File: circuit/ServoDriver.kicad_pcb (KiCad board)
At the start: 2 copper layers, 102.5 x 54.5 mm, 47 parts, among them IC1 TLP521, IC2 TLP521, IC3 TLP521, IC4 TLP521, IC5 TLP521, IC6 TLP521, J1 RJ45_8pin, J2 RJ45_8pin, J3 servo0, J4 servo1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

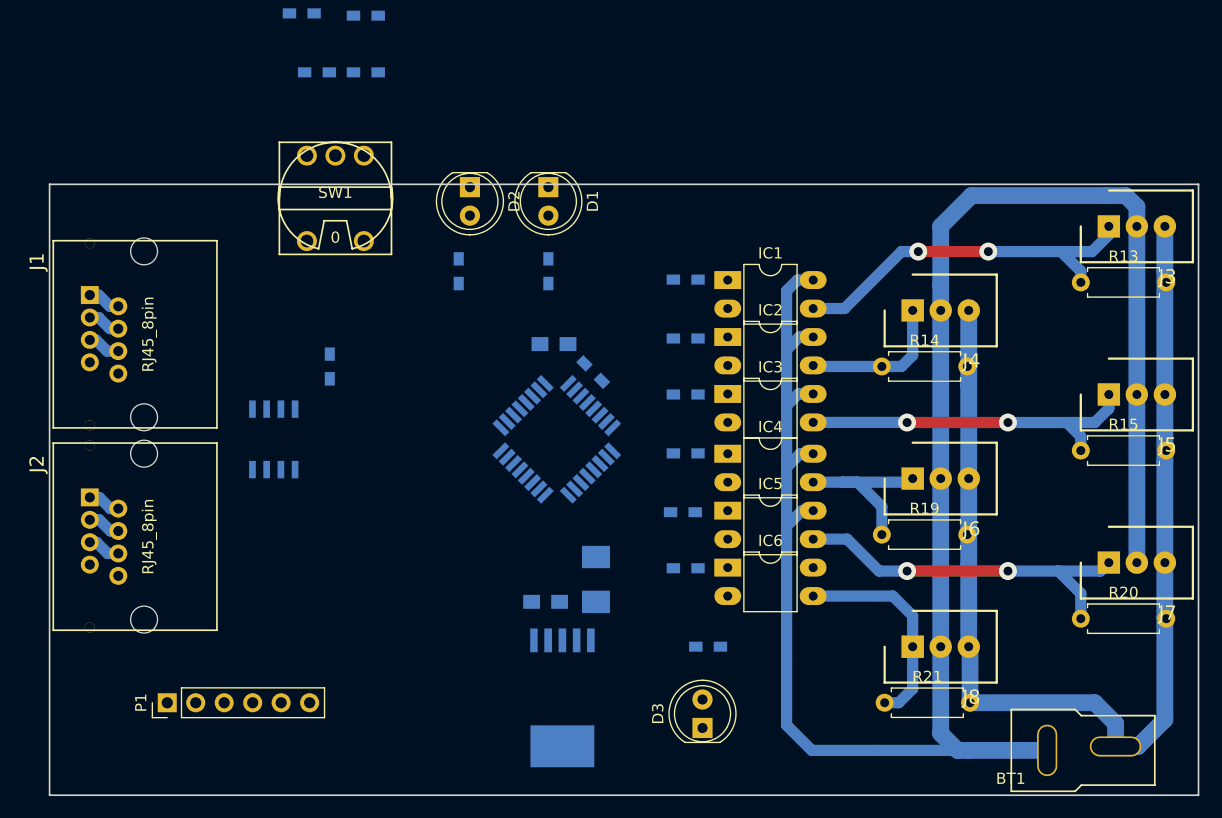
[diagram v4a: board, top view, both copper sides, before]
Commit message: ロータリースイッチとLEDのピンを変更
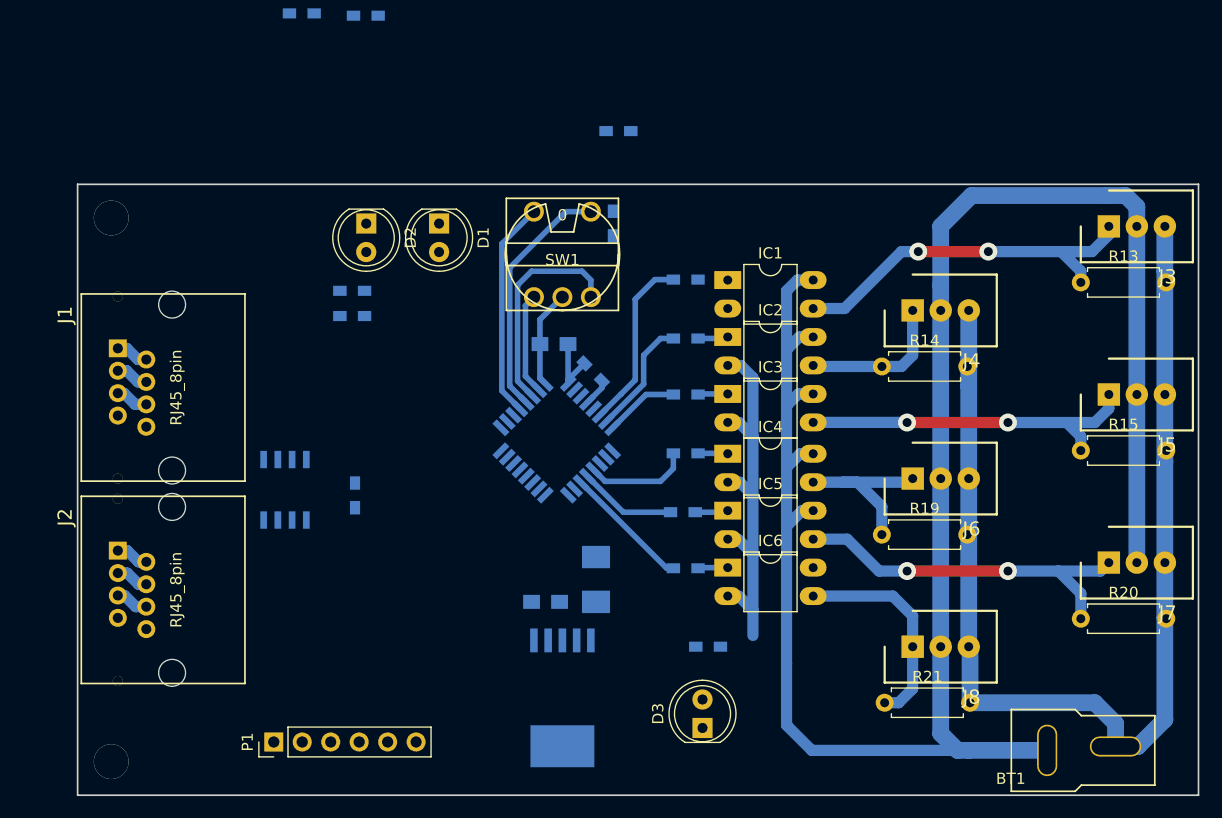
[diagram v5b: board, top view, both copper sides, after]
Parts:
- moved R9 27.4 mm to (132.2, 75.0)
- moved R7 25.8 mm to (131.8, 83.2), turned to 90 degrees
- moved SW1 20.9 mm to (127.2, 86.0), turned to 0 degrees
- moved R1 18.0 mm to (108.5, 91.5), turned to 0 degrees
- moved R5 11.7 mm to (108.8, 107.5)
- moved D1 10.3 mm to (116.2, 83.2)
- moved P1 10.1 mm to (101.5, 129.5)
- moved D2 9.80 mm to (109.8, 83.2)
- moved R2 9.66 mm to (108.5, 89.2), turned to 0 degrees
- moved J1 5.37 mm to (90.1, 97.9)
- moved J2 5.37 mm to (90.1, 115.9)
- moved U2 4.61 mm to (102.5, 107.0)
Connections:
- U1 pad 27: /RotarySW/BIT0 -> Net-(R1-Pad1)
- U1 pad 28: /RotarySW/BIT1 -> /RotarySW/BIT0
- U1 pad 29: /RotarySW/BIT2 -> /RotarySW/BIT1
- U1 pad 30: /RotarySW/BIT3 -> /RotarySW/BIT2
- U1 pad 31: Net-(R1-Pad1) -> /RotarySW/BIT3
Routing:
- net GND: track 6.20 -> 51.7 mm
- net /RotarySW/BIT1: track 0.00 -> 21.9 mm
- net /RotarySW/BIT0: track 0.00 -> 19.4 mm
- net /RotarySW/BIT2: track 0.00 -> 19.4 mm
- net /Servo0: track 0.00 -> 15.8 mm
- net /Servo5: track 0.00 -> 11.4 mm
- net /Servo1: track 0.00 -> 10.6 mm
- net /Servo3: track 0.00 -> 9.36 mm
- net /RotarySW/BIT3: track 0.00 -> 9.09 mm
- net /Servo4: track 0.00 -> 8.76 mm
- net /Servo2: track 0.00 -> 6.65 mm
- net +3V3: track 0.00 -> 5.92 mm
- net Net-(IC5-Pad1): track 0.00 -> 2.96 mm
- net Net-(IC2-Pad1): track 0.00 -> 2.71 mm
- net Net-(IC6-Pad1): track 0.00 -> 2.68 mm
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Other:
- board size 102.5 x 54.5 mm -> 100 x 54.5 mm

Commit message: ロータリースイッチの配線終わり
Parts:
- R9: footprint Resistors_SMD:R_0603_HandSoldering -> Resistors_THT:R_Axial_DIN0207_L6.3mm_D2.5mm_P7.62mm_Horizontal; moved to F.Cu
- moved R8 37.2 mm to (128.8, 92.2)
- moved R6 30.0 mm to (133.2, 83.2), turned to 90 degrees
- moved R9 17.5 mm to (132.2, 92.5), turned to 180 degrees
- moved R1 9.58 mm to (118.0, 90.2), turned to 90 degrees
- moved R2 1.46 mm to (109.8, 90.0), turned to 90 degrees
- moved C1 0.79 mm to (126.8, 94.8)
- moved R4 0.56 mm to (130.2, 97.0)
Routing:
- net +3V3: track 5.92 -> 21.7 mm
- net /RotarySW/BIT0: track 19.4 -> 29.7 mm
- net GND: track 51.7 -> 60.0 mm
- net Net-(IC1-Pad1): track 0.00 -> 2.67 mm
- net /RotarySW/BIT2: track 19.4 -> 21.8 mm
- net /RotarySW/BIT1: track 21.9 -> 23.9 mm

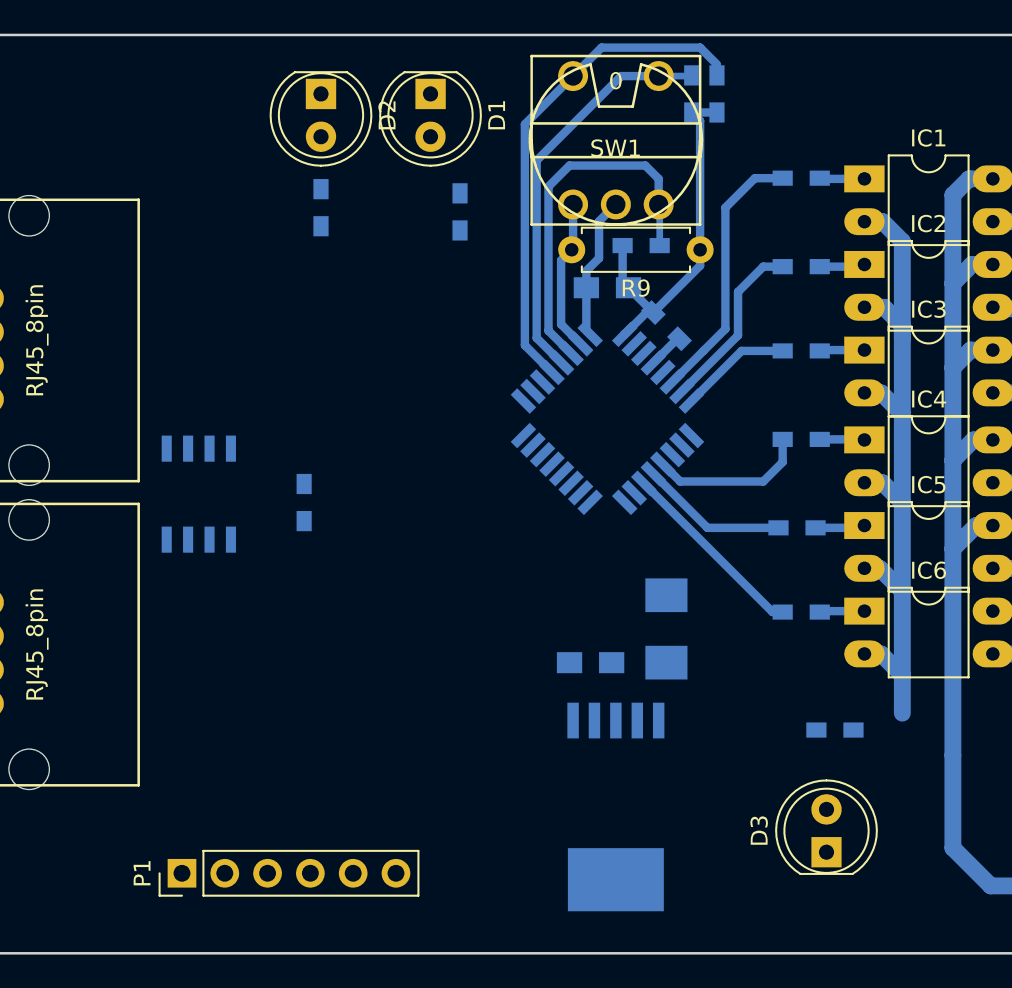
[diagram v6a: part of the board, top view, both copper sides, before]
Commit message: レギュレータまわりの配線完了
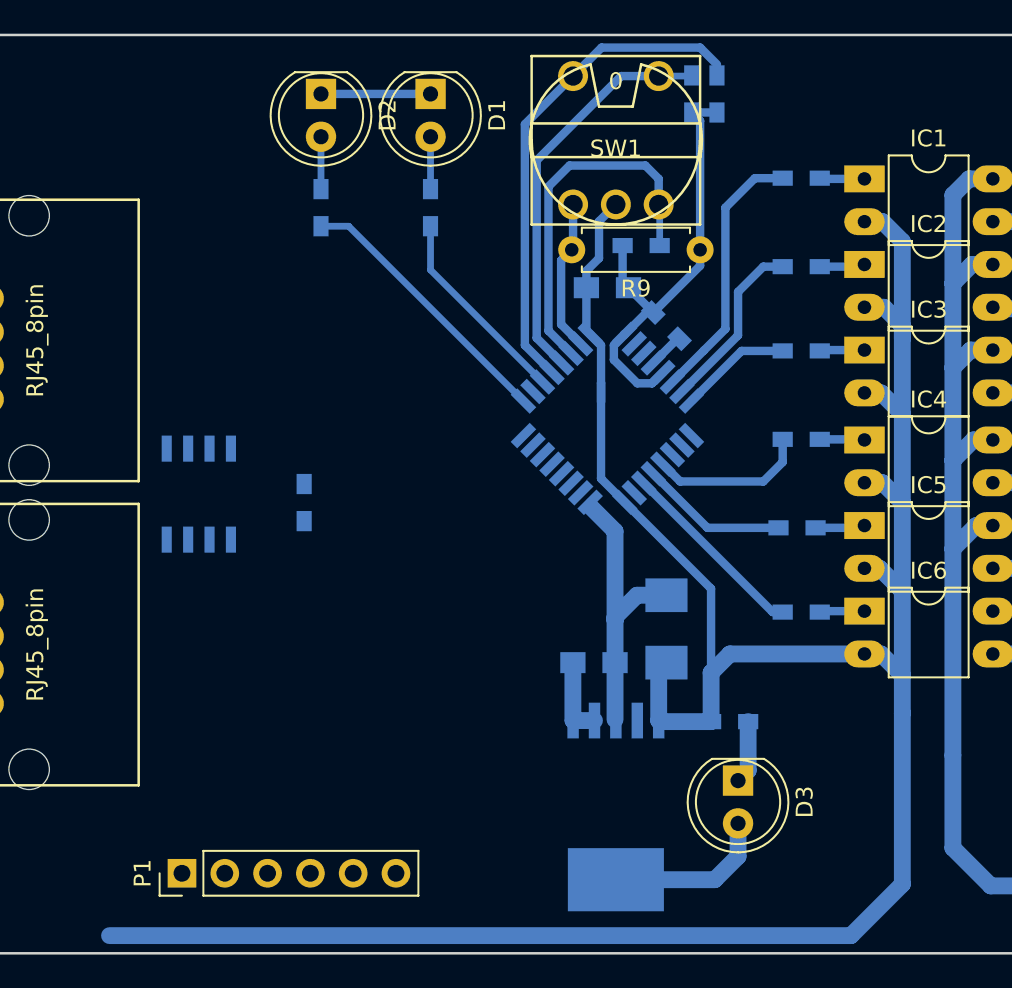
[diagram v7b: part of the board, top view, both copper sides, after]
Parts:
- moved D3 6.75 mm to (134.5, 124.0), turned to 270 degrees
- moved R3 6.27 mm to (134.0, 120.5)
- moved R1 1.77 mm to (116.2, 90.0)
- moved C2 0.20 mm to (126.0, 117.0)
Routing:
- net GND: track 60.0 -> 168.4 mm
- net +3V3: track 21.7 -> 54.4 mm
- net Net-(R2-Pad1): track 0.00 -> 16.3 mm
- net Net-(R1-Pad1): track 0.00 -> 12.0 mm
- net +5V: track 5.91 -> 10.6 mm
- net Net-(D3-Pad1): track 0.00 -> 3.75 mm
- net Net-(D2-Pad2): track 0.00 -> 3.11 mm
- net Net-(D1-Pad2): track 0.00 -> 3.11 mm
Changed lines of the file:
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@@
   (general
     (links 117)
-    (no_connects 42)
-    (area 83.924999 79.674999 184.075001 134.325001)
+    (no_connects 24)
+    (area 70.900002 77.034 191.176192 142.45)
     (thickness 1.6)
     (drawings 7)
-    (tracks 232)
+    (tracks 280)
     (zones 0)
     (modules 47)
@@
   )
   (module Capacitors_SMD:C_0805_HandSoldering (layer B.Cu)
-    (at 125.75 117)
+    (at 125.95 117)
     (descr "Capacitor SMD 0805, hand soldering")
     (tags "capacitor 0805")
@@
   )
   (module LEDs:LED_D5.0mm (layer F.Cu)
-    (at 139.75 128.25 90)
+    (at 134.5 124 270)
     (descr "LED, diameter 5.0mm, 2 pins, http://cdn-reichelt.de/documents/datenblatt/A500/LL-504BC2E-009.pdf")
     (tags "LED diameter 5.0mm 2 pins")
-    (fp_text reference D3 (at 1.27 -3.96 90) (layer F.SilkS)
-      (effects (font (size 1 1) (thickness 0.15)))
-    )
-    (fp_text value LED (at 1.27 3.96 90) (layer F.Fab)
+    (fp_text reference D3 (at 1.27 -3.96 270) (layer F.SilkS)
+      (effects (font (size 1 1) (thickness 0.15)))
+    )
+    (fp_text value LED (at 1.27 3.96 270) (layer F.Fab)
       (effects (font (size 1 1) (thickness 0.15)))
     )
@@
     (fp_line (start 4.5 3.25) (end 4.5 -3.25) (layer F.CrtYd) (width 0.05))
     (fp_line (start 4.5 -3.25) (end -1.95 -3.25) (layer F.CrtYd) (width 0.05))
-    (pad 1 thru_hole rect (at 0 0 90) (size 1.8 1.8) (drill 0.9) (layers *.Cu *.Mask)
+    (pad 1 thru_hole rect (at 0 0 270) (size 1.8 1.8) (drill 0.9) (layers *.Cu *.Mask)
       (net 8 "Net-(D3-Pad1)"))
-    (pad 2 thru_hole circle (at 2.54 0 90) (size 1.8 1.8) (drill 0.9) (layers *.Cu *.Mask)
+    (pad 2 thru_hole circle (at 2.54 0 270) (size 1.8 1.8) (drill 0.9) (layers *.Cu *.Mask)
       (net 3 +3V3))
     (model ${KISYS3DMOD}/LEDs.3dshapes/LED_D5.0mm.wrl
@@
   )
   (module Resistors_SMD:R_0603_HandSoldering (layer B.Cu)
-    (at 118 90.25 90)
+    (at 116.25 90 90)
     (descr "Resistor SMD 0603, hand soldering")
     (tags "resistor 0603")
@@
   )
   (module Resistors_SMD:R_0603_HandSoldering (layer B.Cu)
-    (at 140.25 121 180)
+    (at 134 120.5 180)
     (descr "Resistor SMD 0603, hand soldering")
     (tags "resistor 0603")
@@
   (segment (start 163.5 106) (end 163.5 97.75) (width 1.5) (layer B.Cu) (net 2))
   (segment (start 163.5 97.75) (end 163.5 91) (width 1.5) (layer B.Cu) (net 2))
+  (segment (start 125.724695 107.485103) (end 125.8 107.560408) (width 0.5) (layer B.Cu) (net 3) (status C00000))
+  (segment (start 125.8 107.560408) (end 125.8 107.8) (width 0.5) (layer B.Cu) (net 3) (status 400000))
+  (segment (start 125.8 107.8) (end 127.2 109.2) (width 1) (layer B.Cu) (net 3))
+  (segment (start 127.2 109.2) (end 127.2 114.5) (width 1) (layer B.Cu) (net 3))
+  (segment (start 127.2 117) (end 127.2 114.5) (width 1) (layer B.Cu) (net 3))
+  (segment (start 127.2 114.5) (end 127.2 114.3) (width 1) (layer B.Cu) (net 3))
+  (segment (start 128.5 113) (end 130.25 113) (width 1) (layer B.Cu) (net 3))
+  (segment (start 127.2 114.3) (end 128.5 113) (width 1) (layer B.Cu) (net 3))
+  (segment (start 134.5 126.54) (end 134.5 128.5) (width 1) (layer B.Cu) (net 3))
+  (segment (start 133.118 129.882) (end 127.25 129.882) (width 1) (layer B.Cu) (net 3))
+  (segment (start 134.5 128.5) (end 133.118 129.882) (width 1) (layer B.Cu) (net 3))
+  (segment (start 127.25052 120.4365) (end 127.2 120.38598) (width 0.5) (layer B.Cu) (net 3))
+  (segment (start 127.2 120.38598) (end 127.2 117) (width 1) (layer B.Cu) (net 3))
+  (segment (start 127.13084 99.03084) (end 128.522103 100.422103) (width 0.5) (layer B.Cu) (net 3))
+  (segment (start 128.522103 100.422103) (end 129.393583 100.422103) (width 0.5) (layer B.Cu) (net 3))
+  (segment (start 129.393583 100.422103) (end 129.401652 100.414034) (width 0.5) (layer B.Cu) (net 3))
+  (segment (start 129.401652 100.414034) (end 130.038047 99.777639) (width 0.5) (layer B.Cu) (net 3))
+  (segment (start 127.13084 98.159362) (end 127.13084 99.03084) (width 0.5) (layer B.Cu) (net 3))
+  (segment (start 127.775305 97.514897) (end 127.13084 98.159362) (width 0.5) (layer B.Cu) (net 3))
   (segment (start 127.775305 97.514897) (end 129.068019 96.222183) (width 0.5) (layer B.Cu) (net 3))
   (segment (start 131.75 84.35) (end 133.25 84.35) (width 0.5) (layer B.Cu) (net 3))
@@
   (segment (start 129.068019 96.222183) (end 129.472183 96.222183) (width 0.5) (layer B.Cu) (net 3))
   (segment (start 127.775305 97.514897) (end 127.75 97.489592) (width 0.5) (layer B.Cu) (net 3))
+  (segment (start 144.25 120) (end 144.25 130.15) (width 1) (layer B.Cu) (net 4))
+  (segment (start 144.25 117.75) (end 144.25 120) (width 1) (layer B.Cu) (net 4))
+  (segment (start 141.2 133.2) (end 97.2 133.2) (width 1) (layer B.Cu) (net 4))
+  (segment (start 144.25 130.15) (end 141.2 133.2) (width 1) (layer B.Cu) (net 4))
+  (segment (start 142.002 116.484) (end 134.016 116.484) (width 1) (layer B.Cu) (net 4) (status 400000))
+  (segment (start 134.016 116.484) (end 132.9 117.6) (width 1) (layer B.Cu) (net 4))
+  (segment (start 127.775305 107.485103) (end 132.9 112.609798) (width 0.5) (layer B.Cu) (net 4) (status 400000))
+  (segment (start 132.9 112.609798) (end 132.9 117.6) (width 0.5) (layer B.Cu) (net 4))
+  (segment (start 132.9 117.6) (end 132.9 120.5) (width 1) (layer B.Cu) (net 4) (status 800000))
+  (segment (start 132.9 120.5) (end 129.85402 120.5) (width 1) (layer B.Cu) (net 4))
+  (segment (start 129.85402 120.5) (end 129.79052 120.4365) (width 1) (layer B.Cu) (net 4))
+  (segment (start 129.79052 120.4365) (end 129.79052 117.45948) (width 1) (layer B.Cu) (net 4))
+  (segment (start 129.79052 117.45948) (end 130.25 117) (width 1) (layer B.Cu) (net 4))
+  (segment (start 126.36916 100.4) (end 126.36916 101.53084) (width 0.5) (layer B.Cu) (net 4))
+  (segment (start 126.36916 98.159362) (end 126.36916 100.4) (width 0.5) (layer B.Cu) (net 4))
+  (segment (start 126.36916 100.4) (end 126.36916 106.078958) (width 0.5) (layer B.Cu) (net 4))
+  (segment (start 126.36916 106.078958) (end 127.775305 107.485103) (width 0.5) (layer B.Cu) (net 4))
+  (segment (start 125.724695 97.514897) (end 126.36916 98.159362) (width 0.5) (layer B.Cu) (net 4))
+  (segment (start 109.75 83.25) (end 116.25 83.25) (width 0.5) (layer B.Cu) (net 4))
   (segment (start 144.25 97.75) (end 144.25 92) (width 1) (layer B.Cu) (net 4))
   (segment (start 144.25 92) (end 143.08 90.83) (width 1) (layer B.Cu) (net 4))
@@
   (segment (start 144.25 107.5) (end 144.25 112.75) (width 1) (layer B.Cu) (net 4))
   (segment (start 144.25 112.75) (end 144.25 117.75) (width 1) (layer B.Cu) (net 4))
-  (segment (start 144.25 117.75) (end 144.25 120) (width 1) (layer B.Cu) (net 4))
   (segment (start 87.59 116.43) (end 88.18 116.43) (width 1) (layer B.Cu) (net 4))
   (segment (start 88.18 116.43) (end 89.18 117.43) (width 1) (layer B.Cu) (net 4))
@@
   (segment (start 89.13 99.38) (end 90.13 99.38) (width 1) (layer B.Cu) (net 4))
   (segment (start 87.59 98.38) (end 87.88 98.38) (width 1) (layer B.Cu) (net 4))
+  (segment (start 125.98052 120.4365) (end 124.71052 120.4365) (width 1) (layer B.Cu) (net 5))
+  (segment (start 124.71052 120.4365) (end 124.7 120.42598) (width 0.5) (layer B.Cu) (net 5))
+  (segment (start 124.7 120.42598) (end 124.7 117) (width 1) (layer B.Cu) (net 5))
   (segment (start 87.59 114.43) (end 88.43 114.43) (width 1) (layer B.Cu) (net 5))
   (segment (start 88.43 114.43) (end 89.43 115.43) (width 1) (layer B.Cu) (net 5))
@@
   (segment (start 89.38 97.38) (end 88.38 96.38) (width 1) (layer B.Cu) (net 5))
   (segment (start 88.38 96.38) (end 87.59 96.38) (width 1) (layer B.Cu) (net 5))
+  (segment (start 116.25 85.79) (end 116.25 88.9) (width 0.4) (layer B.Cu) (net 6))
+  (segment (start 109.75 85.79) (end 109.75 88.9) (width 0.4) (layer B.Cu) (net 7))
+  (segment (start 135.1 120.5) (end 135.1 123.4) (width 1) (layer B.Cu) (net 8))
+  (segment (start 135.1 123.4) (end 134.5 124) (width 1) (layer B.Cu) (net 8))
   (segment (start 132.473528 98.473528) (end 133.75 97.197056) (width 0.5) (layer B.Cu) (net 9))
   (segment (start 133.75 90) (end 135.5 88.25) (width 0.5) (layer B.Cu) (net 9))
@@
   (segment (start 129.472361 99.211953) (end 130.906497 97.777817) (width 0.5) (layer B.Cu) (net 27))
   (segment (start 130.906497 97.777817) (end 131.027817 97.777817) (width 0.5) (layer B.Cu) (net 27))
+  (segment (start 116.25 91.1) (end 116.25 93.697056) (width 0.4) (layer B.Cu) (net 29))
+  (segment (start 116.25 93.697056) (end 122.896268 100.343324) (width 0.4) (layer B.Cu) (net 29))
+  (segment (start 121.764897 101.474695) (end 111.390202 91.1) (width 0.4) (layer B.Cu) (net 30))
+  (segment (start 111.390202 91.1) (end 109.75 91.1) (width 0.4) (layer B.Cu) (net 30))
   (segment (start 124.71 82.19) (end 126.4 80.5) (width 0.5) (layer B.Cu) (net 32))
   (segment (start 133.25 81.5) (end 133.25 82.15) (width 0.4) (layer B.Cu) (net 32))

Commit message: 配線完了
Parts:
- U2: footprint Housings_SOIC:SOIC-8_3.9x4.9mm_Pitch1.27mm -> Housings_DIP:DIP-8_W7.62mm_Socket_LongPads; moved to F.Cu
- moved U2 12.6 mm to (114.5, 111.0), turned to 180 degrees
- moved J1 7.87 mm to (98.0, 98.0), turned to 270 degrees
- moved J2 7.87 mm to (98.0, 116.0), turned to 270 degrees
- moved P1 5.10 mm to (96.5, 128.5)
- moved R5 3.91 mm to (110.5, 111.0), turned to 0 degrees
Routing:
- net GND: track 168.4 -> 294.3 mm
- net +5V: track 10.6 -> 71.8 mm, vias 0 -> 2
- net Net-(J1-Pad8): track 0.00 -> 37.9 mm, vias 0 -> 2
- net Net-(J1-Pad7): track 0.00 -> 34.3 mm, vias 0 -> 2
- net +3V3: track 54.4 -> 85.5 mm, vias 0 -> 2
- net +12V: track 5.91 -> 31.5 mm
- net /CAN_TxD: track 0.00 -> 17.6 mm, vias 0 -> 2
- net /CAN_RxD: track 0.00 -> 11.2 mm
- net /SWDIO: track 0.00 -> 3.83 mm
- net Net-(R5-Pad1): track 0.00 -> 2.52 mm
- net /SWCLK: track 0.00 -> 2.09 mm
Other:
- board size 100 x 54.5 mm -> 95 x 54.5 mm
